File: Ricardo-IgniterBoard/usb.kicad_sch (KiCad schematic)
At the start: 8 parts, among them J2 USB_C_Receptacle_USB2.0

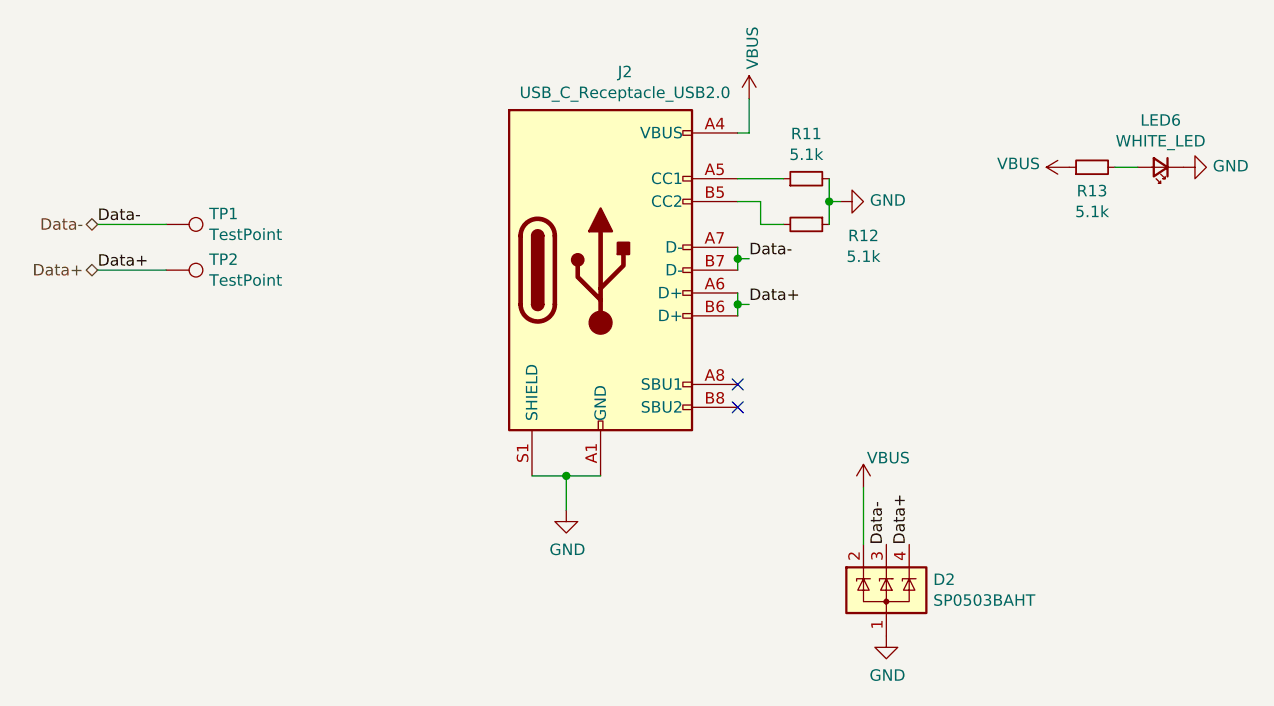
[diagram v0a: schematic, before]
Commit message: Assigning components
And added the thermocouple
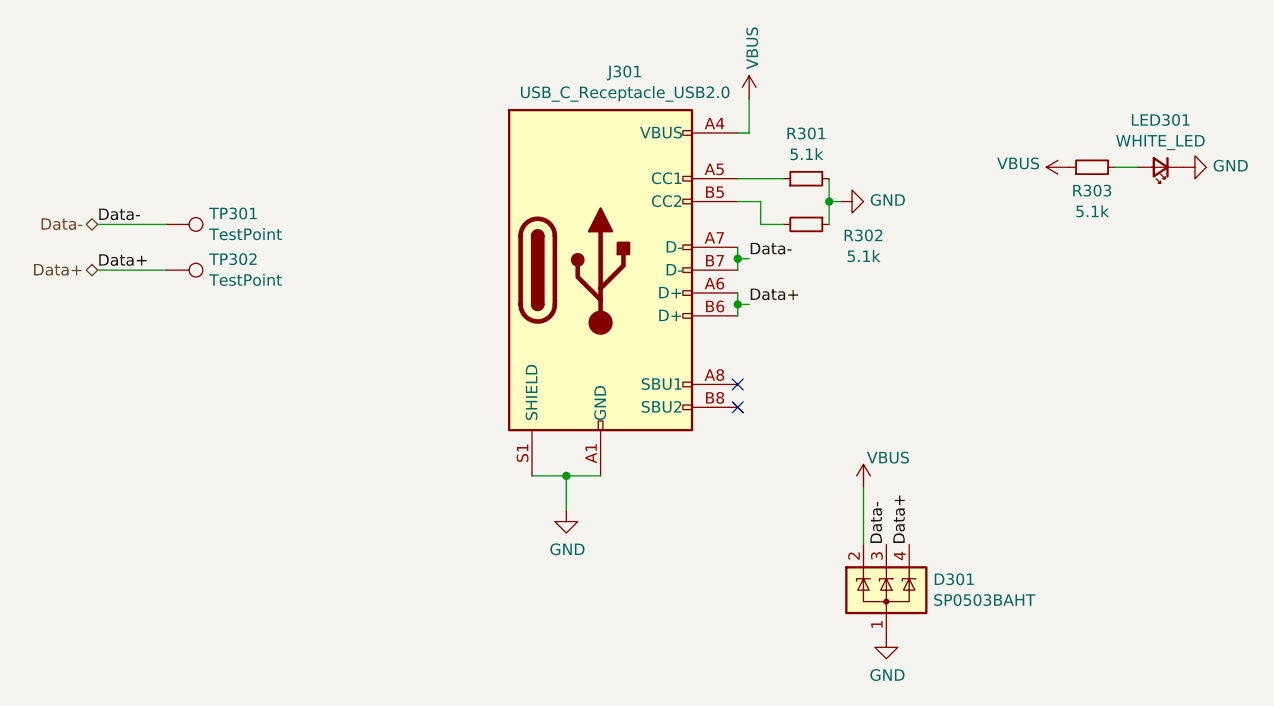
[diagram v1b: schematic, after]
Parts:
- renumbered D2 to D301, J2 to J301, LED6 to LED301, R11 to R301, R12 to R302, R13 to R303, TP1 to TP301, TP2 to TP302
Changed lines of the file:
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@@
 		(on_board yes)
 		(dnp no)
-		(property "Reference" "R12"
+		(property "Reference" "R302"
 			(at 129.54 100.33 90)
 			(effects
@@
 			(project "RicardoTemplate"
 				(path "/7db990e4-92e1-4f99-b4d2-435bbec1ba83/00000000-0000-0000-0000-000061925999"
-					(reference "R12")
+					(reference "R302")
 					(unit 1)
 				)
@@
 		(on_board yes)
 		(dnp no)
-		(property "Reference" "R11"
+		(property "Reference" "R301"
 			(at 123.19 89.0016 90)
 			(effects
@@
 			(project "RicardoTemplate"
 				(path "/7db990e4-92e1-4f99-b4d2-435bbec1ba83/00000000-0000-0000-0000-000061925999"
-					(reference "R11")
+					(reference "R301")
 					(unit 1)
 				)
@@
 		(on_board yes)
 		(dnp no)
-		(property "Reference" "J2"
+		(property "Reference" "J301"
 			(at 103.0478 82.1182 0)
 			(effects
@@
 			(project "RicardoTemplate"
 				(path "/7db990e4-92e1-4f99-b4d2-435bbec1ba83/00000000-0000-0000-0000-000061925999"
-					(reference "J2")
+					(reference "J301")
 					(unit 1)
 				)
@@
 		(on_board yes)
 		(dnp no)
-		(property "Reference" "D2"
+		(property "Reference" "D301"
 			(at 137.287 138.5316 0)
 			(effects
@@
 			(project "RicardoTemplate"
 				(path "/7db990e4-92e1-4f99-b4d2-435bbec1ba83/00000000-0000-0000-0000-000061925999"
-					(reference "D2")
+					(reference "D301")
 					(unit 1)
 				)
@@
 		(on_board yes)
 		(dnp no)
-		(property "Reference" "TP1"
+		(property "Reference" "TP301"
 			(at 56.8452 97.8916 90)
 			(effects
@@
 			(project "RicardoTemplate"
 				(path "/7db990e4-92e1-4f99-b4d2-435bbec1ba83/00000000-0000-0000-0000-000061925999"
-					(reference "TP1")
+					(reference "TP301")
 					(unit 1)
 				)
@@
 		(on_board yes)
 		(dnp no)
-		(property "Reference" "TP2"
+		(property "Reference" "TP302"
 			(at 56.8452 102.9716 90)
 			(effects
@@
 			(project "RicardoTemplate"
 				(path "/7db990e4-92e1-4f99-b4d2-435bbec1ba83/00000000-0000-0000-0000-000061925999"
-					(reference "TP2")
+					(reference "TP302")
 					(unit 1)
 				)
@@
 		(on_board yes)
 		(dnp no)
-		(property "Reference" "LED6"
+		(property "Reference" "LED301"
 			(at 162.56 87.503 0)
 			(effects
@@
 			(project "RicardoTemplate"
 				(path "/7db990e4-92e1-4f99-b4d2-435bbec1ba83/00000000-0000-0000-0000-000061925999"
-					(reference "LED6")
+					(reference "LED301")
 					(unit 1)
 				)
@@
 		(on_board yes)
 		(dnp no)
-		(property "Reference" "R13"
+		(property "Reference" "R303"
 			(at 154.94 95.3516 90)
 			(effects
@@
 			(project "RicardoTemplate"
 				(path "/7db990e4-92e1-4f99-b4d2-435bbec1ba83/00000000-0000-0000-0000-000061925999"
-					(reference "R13")
-					(unit 1)
-				)
+					(reference "R303")
+					(unit 1)
+				)
